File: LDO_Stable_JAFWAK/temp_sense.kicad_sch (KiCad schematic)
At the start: 6 parts, among them U2 TMP235A2DBZR

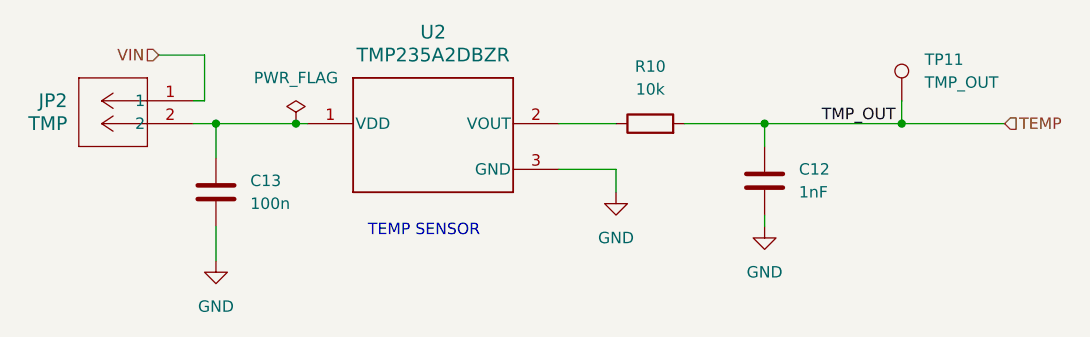
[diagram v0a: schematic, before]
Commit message: Several Changes
Moved temp sensor closer to chip
Add silkscreen
Moved capacitors closer to chip
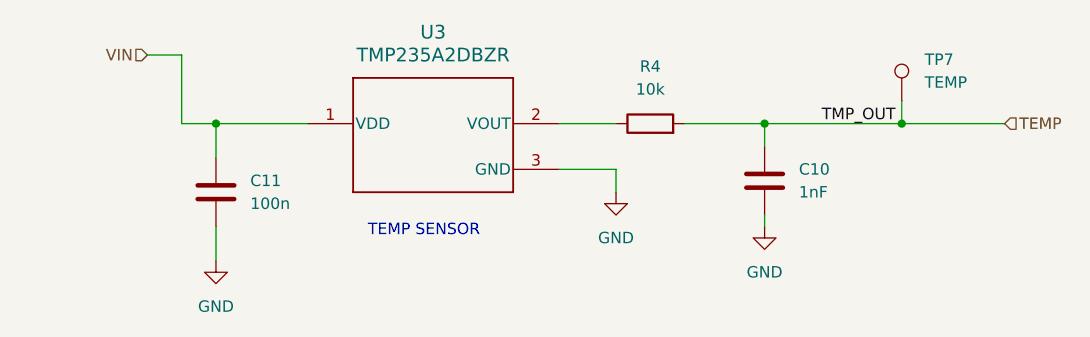
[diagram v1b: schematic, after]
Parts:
- removed JP2: TMP, Connector_PinHeader_2.54mm:PinHeader_1x02_P2.54mm_Vertical, symbol PEC02SAAN:PEC02SAAN
- C10: renamed from C12; KiLib_Generator (none) -> SMD_2terminal_chip_molded
- C11: renamed from C13; KiLib_Generator (none) -> SMD_2terminal_chip_molded
- R4: renamed from R10; KiLib_Generator (none) -> SMD_2terminal_chip_molded
- TP7: renamed from TP11; value TMP_OUT -> TEMP
- renumbered U2 to U3
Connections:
- net VIN: now also C11.1, U3.1 (VDD)
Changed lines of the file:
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@@
 		(color 0 0 0 0)
 	)
-	(junction
-		(at 111.76 77.47)
-		(diameter 0)
-		(color 0 0 0 0)
-	)
 	(wire
 		(pts
@@
 	(wire
 		(pts
-			(xy 96.52 69.85) (xy 101.6 69.85)
+			(xy 95.25 69.85) (xy 99.06 69.85)
 		)
 		(stroke
@@
 	(wire
 		(pts
-			(xy 101.6 74.93) (xy 100.33 74.93)
-		)
-		(stroke
-			(width 0)
-			(type default)
-		)
-	)
-	(wire
-		(pts
-			(xy 101.6 69.85) (xy 101.6 74.93)
+			(xy 99.06 69.85) (xy 99.06 77.47)
 		)
 		(stroke
@@
 	(wire
 		(pts
-			(xy 102.87 77.47) (xy 111.76 77.47)
-		)
-		(stroke
-			(width 0)
-			(type default)
-		)
-	)
-	(wire
-		(pts
 			(xy 163.83 77.47) (xy 179.07 77.47)
 		)
@@
 	(wire
 		(pts
-			(xy 100.33 77.47) (xy 102.87 77.47)
+			(xy 99.06 77.47) (xy 102.87 77.47)
 		)
 		(stroke
@@
 	(wire
 		(pts
-			(xy 111.76 77.47) (xy 113.03 77.47)
+			(xy 102.87 77.47) (xy 113.03 77.47)
 		)
 		(stroke
@@
 	(hierarchical_label "VIN"
 		(shape input)
-		(at 96.52 69.85 180)
+		(at 95.25 69.85 180)
 		(effects
 			(font
@@
 		(dnp no)
 		(fields_autoplaced yes)
-		(property "Reference" "TP11"
+		(property "Reference" "TP7"
 			(at 181.61 70.3579 0)
 			(show_name no)
@@
 			)
 		)
-		(property "Value" "TMP_OUT"
+		(property "Value" "TEMP"
 			(at 181.61 72.8979 0)
 			(show_name no)
@@
 			(project "LDO_Stable_JAFWAK"
 				(path "/e797984e-8841-4b55-a934-93c9429b6b10/ff44080c-9e84-4b6d-8105-be8b15417474"
-					(reference "TP11")
+					(reference "TP7")
 					(unit 1)
 				)
@@
 		(dnp no)
 		(fields_autoplaced yes)
-		(property "Reference" "R10"
+		(property "Reference" "R4"
 			(at 151.13 71.12 90)
 			(show_name no)
@@
 		)
 		(property "Distrbuter Link 2" "https://www.mouser.com/en/ProductDetail/YAGEO/RC0805FR-0710KL?qs=7bY8808IzHq6vrU3BeiiYw%3D%3D"
+			(at 151.13 77.47 0)
+			(hide yes)
+			(show_name no)
+			(do_not_autoplace no)
+			(effects
+				(font
+					(size 1.27 1.27)
+				)
+			)
+		)
+		(property "KiLib_Generator" "SMD_2terminal_chip_molded"
 			(at 151.13 77.47 0)
 			(hide yes)
@@
 			(project "LDO_Stable_JAFWAK"
 				(path "/e797984e-8841-4b55-a934-93c9429b6b10/ff44080c-9e84-4b6d-8105-be8b15417474"
-					(reference "R10")
+					(reference "R4")
 					(unit 1)
 				)
@@
 		(dnp no)
 		(fields_autoplaced yes)
-		(property "Reference" "C13"
+		(property "Reference" "C11"
 			(at 106.68 83.8199 0)
 			(show_name no)
@@
 		)
 		(property "Distributer Link 2" "https://www.mouser.com/en/ProductDetail/KEMET/C0805C102K5RACTU?qs=nyGfpDADWE7v2OrzBT8v1g%3D%3D"
+			(at 102.87 85.09 0)
+			(hide yes)
+			(show_name no)
+			(do_not_autoplace no)
+			(effects
+				(font
+					(size 1.27 1.27)
+				)
+			)
+		)
+		(property "KiLib_Generator" "SMD_2terminal_chip_molded"
 			(at 102.87 85.09 0)
 			(hide yes)
@@
 			(project "LDO_Stable_JAFWAK"
 				(path "/e797984e-8841-4b55-a934-93c9429b6b10/ff44080c-9e84-4b6d-8105-be8b15417474"
-					(reference "C13")
+					(reference "C11")
 					(unit 1)
 				)
@@
 		(dnp no)
 		(fields_autoplaced yes)
-		(property "Reference" "C12"
+		(property "Reference" "C10"
 			(at 167.64 82.5499 0)
 			(show_name no)
@@
 		)
 		(property "Distributer Link 2" "https://www.mouser.com/en/ProductDetail/KEMET/C0805C102K5RACTU?qs=nyGfpDADWE7v2OrzBT8v1g%3D%3D"
+			(at 163.83 83.82 0)
+			(hide yes)
+			(show_name no)
+			(do_not_autoplace no)
+			(effects
+				(font
+					(size 1.27 1.27)
+				)
+			)
+		)
+		(property "KiLib_Generator" "SMD_2terminal_chip_molded"
 			(at 163.83 83.82 0)
 			(hide yes)
@@
 			(project "LDO_Stable_JAFWAK"
 				(path "/e797984e-8841-4b55-a934-93c9429b6b10/ff44080c-9e84-4b6d-8105-be8b15417474"
-					(reference "C12")
+					(reference "C10")
 					(unit 1)
 				)
@@
 	)
 	(symbol
-		(lib_id "PEC02SAAN:PEC02SAAN")
-		(at 100.33 74.93 0)
-		(mirror y)
-		(unit 1)
-		(body_style 1)
-		(exclude_from_sim no)
-		(in_bom yes)
-		(on_board yes)
-		(in_pos_files yes)
-		(dnp no)
-		(property "Reference" "JP2"
-			(at 86.36 74.9299 0)
-			(show_name no)
-			(do_not_autoplace no)
-			(effects
-				(font
-					(size 1.524 1.524)
-				)
-				(justify left)
-			)
-		)
-		(property "Value" "TMP"
-			(at 86.36 77.4699 0)
-			(show_name no)
-			(do_not_autoplace no)
-			(effects
-				(font
-					(size 1.524 1.524)
-				)
-				(justify left)
-			)
-		)
-		(property "Footprint" "Connector_PinHeader_2.54mm:PinHeader_1x02_P2.54mm_Vertical"
-			(at 100.33 74.93 0)
-			(hide yes)
-			(show_name no)
-			(do_not_autoplace no)
-			(effects
-				(font
-					(size 1.27 1.27)
-					(italic yes)
-				)
-			)
-		)
-		(property "Datasheet" "PEC02SAAN"
-			(at 100.33 74.93 0)
-			(hide yes)
-			(show_name no)
-			(do_not_autoplace no)
-			(effects
-				(font
-					(size 1.27 1.27)
-					(italic yes)
-				)
-			)
-		)
-		(property "Description" "CONN HEADER VERT 2POS 2.54MM"
-			(at 100.33 74.93 0)
-			(hide yes)
-			(show_name no)
-			(do_not_autoplace no)
-			(effects
-				(font
-					(size 1.27 1.27)
-				)
-			)
-		)
-		(property "Manufacturer" "Sullins Connector Solutions"
-			(at 100.33 74.93 0)
-			(hide yes)
-			(show_name no)
-			(do_not_autoplace no)
-			(effects
-				(font
-					(size 1.27 1.27)
-				)
-			)
-		)
-		(property "Manufacturer Part Number" "PEC02SAAN"
-			(at 100.33 74.93 0)
-			(hide yes)
-			(show_name no)
-			(do_not_autoplace no)
-			(effects
-				(font
-					(size 1.27 1.27)
-				)
-			)
-		)
-		(property "Distributer Link 1" "https://www.digikey.com/en/products/detail/sullins-connector-solutions/PEC02SAAN/859155?s=N4IgTCBcDaIAoFEDCAGMBlAgpgciAugL5A"
-			(at 100.33 74.93 0)
-			(hide yes)
-			(show_name no)
-			(do_not_autoplace no)
-			(effects
-				(font
-					(size 1.27 1.27)
-				)
-			)
-		)
-		(property "Distributer Link 2" ""
-			(at 100.33 74.93 0)
-			(hide yes)
-			(show_name no)
-			(do_not_autoplace no)
-			(effects
-				(font
-					(size 1.27 1.27)
-				)
-			)
-		)
-		(pin "1"
-		)
-		(pin "2"
-		)
-		(instances
-			(project "LDO_Stable_JAFWAK"
-				(path "/e797984e-8841-4b55-a934-93c9429b6b10/ff44080c-9e84-4b6d-8105-be8b15417474"
-					(reference "JP2")
-					(unit 1)
-				)
-			)
-		)
-	)
-	(symbol
-		(lib_id "power:PWR_FLAG")
-		(at 111.76 77.47 0)
-		(unit 1)
-		(body_style 1)
-		(exclude_from_sim no)
-		(in_bom yes)
-		(on_board yes)
-		(in_pos_files yes)
-		(dnp no)
-		(fields_autoplaced yes)
-		(property "Reference" "#FLG07"
-			(at 111.76 75.565 0)
-			(hide yes)
-			(show_name no)
-			(do_not_autoplace no)
-			(effects
-				(font
-					(size 1.27 1.27)
-				)
-			)
-		)
-		(property "Value" "PWR_FLAG"
-			(at 111.76 72.39 0)
-			(show_name no)
-			(do_not_autoplace no)
-			(effects
-				(font
-					(size 1.27 1.27)
-				)
-			)
-		)
-		(property "Footprint" ""
-			(at 111.76 77.47 0)
-			(hide yes)
-			(show_name no)
-			(do_not_autoplace no)
-			(effects
-				(font
-					(size 1.27 1.27)
-				)
-			)
-		)
-		(property "Datasheet" ""
-			(at 111.76 77.47 0)
-			(hide yes)
-			(show_name no)
-			(do_not_autoplace no)
-			(effects
-				(font
-					(size 1.27 1.27)
-				)
-			)
-		)
-		(property "Description" "Special symbol for telling ERC where power comes from"
-			(at 111.76 77.47 0)
-			(hide yes)
-			(show_name no)
-			(do_not_autoplace no)
-			(effects
-				(font
-					(size 1.27 1.27)
-				)
-			)
-		)
-		(pin "1"
-		)
-		(instances
-			(project "LDO_Stable_JAFWAK"
-				(path "/e797984e-8841-4b55-a934-93c9429b6b10/ff44080c-9e84-4b6d-8105-be8b15417474"
-					(reference "#FLG07")
-					(unit 1)
-				)
-			)
-		)
-	)
-	(symbol
 		(lib_id "TMP235A2DBZR:TMP235A2DBZR")
 		(at 113.03 77.47 0)
@@
 		(dnp no)
 		(fields_autoplaced yes)
-		(property "Reference" "U2"
+		(property "Reference" "U3"
 			(at 127 67.31 0)
 			(show_name no)
@@
 			(project "LDO_Stable_JAFWAK"
 				(path "/e797984e-8841-4b55-a934-93c9429b6b10/ff44080c-9e84-4b6d-8105-be8b15417474"
-					(reference "U2")
+					(reference "U3")
 					(unit 1)
 				)
